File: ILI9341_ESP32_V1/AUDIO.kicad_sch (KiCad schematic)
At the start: 19 parts, among them CN1 PJ-3043-B, J6 Conn_01x05_Pin, J8 Conn_01x05_Socket, Q3 BC817, U3 PAM8406D

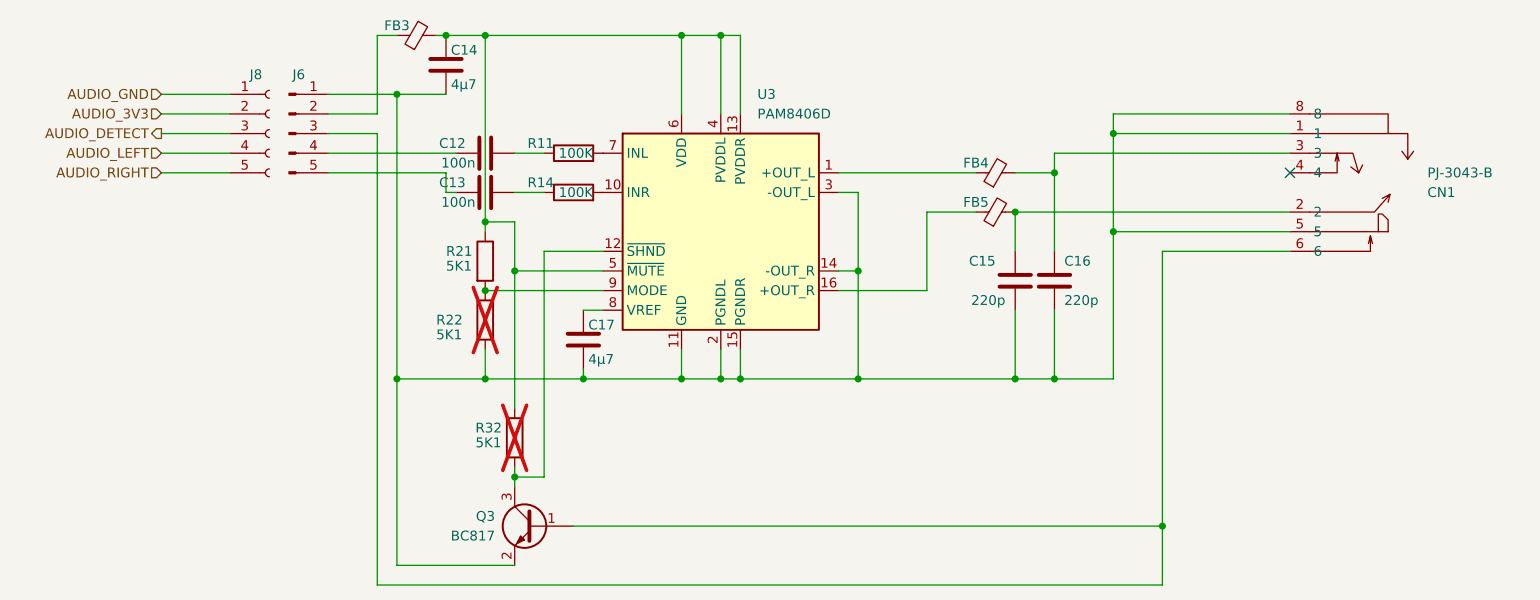
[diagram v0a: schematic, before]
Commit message: update cardridge grabber funktion
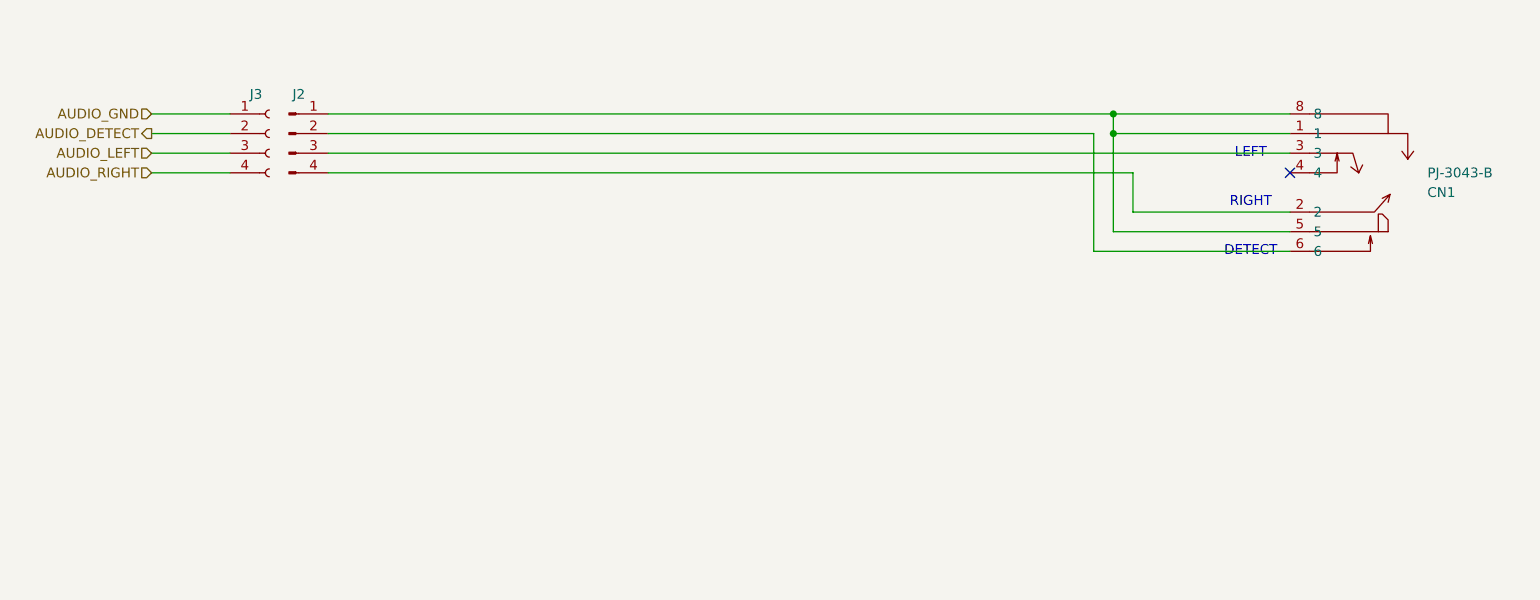
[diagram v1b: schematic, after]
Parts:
- removed C12, C13: 100n, Capacitor_SMD:C_1206_3216Metric, symbol Device:C
- removed C14, C17: 4µ7, Capacitor_SMD:C_1206_3216Metric, symbol Device:C
- removed C15, C16: 220p, Capacitor_SMD:C_0603_1608Metric, symbol Device:C
- removed FB3, FB4, FB5: FerriteBead_Small, Inductor_SMD:L_0805_2012Metric, symbol Device:FerriteBead_Small
- removed J6: Conn_01x05_Pin, Connector_PinHeader_2.00mm:PinHeader_1x05_P2.00mm_Vertical, symbol Connector:Conn_01x05_Pin
- removed J8: Conn_01x05_Socket, Connector_PinHeader_2.00mm:PinHeader_1x05_P2.00mm_Vertical, symbol Connector:Conn_01x05_Socket
- removed Q3: BC817, Package_TO_SOT_SMD:SOT-23, symbol Transistor_BJT:BC817
- removed R11, R14: 100K, Resistor_SMD:R_0603_1608Metric_Pad0.98x0.95mm_HandSolder, symbol Device:R
- removed R21, R22, R32: 5K1, Resistor_SMD:R_0603_1608Metric, symbol Device:R
- removed U3: PAM8406D, Package_SO:SOP-16_3.9x9.9mm_P1.27mm, symbol Amplifier_Audio:PAM8406D
- added J2: Conn_01x04_Pin, Connector_PinHeader_2.00mm:PinHeader_1x04_P2.00mm_Vertical, symbol Connector:Conn_01x04_Pin
- added J3: Conn_01x04_Socket, Connector_PinHeader_2.00mm:PinHeader_1x04_P2.00mm_Vertical, symbol Connector:Conn_01x04_Socket
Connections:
- net AUDIO_DETECT: now also J3.2 (Pin_2)
- net AUDIO_GND: now also J3.1 (Pin_1)
- net AUDIO_LEFT: now also J3.3 (Pin_3)
- net AUDIO_RIGHT: now also J3.4 (Pin_4)
- net at CN1.6: now also J2.2 (Pin_2)
- net at CN1.1, CN1.5, CN1.8: now also J2.1 (Pin_1)
- net at CN1.3: now also J2.3 (Pin_3)
- net at CN1.2: now also J2.4 (Pin_4)
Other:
- note added: "DETECT"
- note added: "LEFT"
- note added: "RIGHT"
